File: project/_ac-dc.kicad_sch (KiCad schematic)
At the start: 27 parts

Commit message: adding more things and specifying components
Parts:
- removed R? (x2): 560K, symbol Device:R
- added C? (x2): 470n, symbol Device:C
- added C? (x2): 2n2, symbol Device:C
- added PS?: PSU 12V 1A, Converter_ACDC:Converter_ACDC_HiLink_HLK-PMxx, symbol Converter_ACDC:HLK-PM01
- added R? (x8): 220k, Resistor_SMD:R_0805_2012Metric_Pad1.20x1.40mm_HandSolder, symbol Device:R
- added RV?: 10D431K, Varistor:RV_Disc_D12mm_W5.4mm_P7.5mm, symbol Device:Varistor
- added TH?: 5D-15, Capacitor_THT:C_Disc_D12.5mm_W5.0mm_P7.50mm, symbol Device:Thermistor_NTC
- C? (x4): value 470u/200v -> 470u; Value2 (none) -> 200v
- C? (x10): value 47u/400v -> 47u; Value2 (none) -> 400v
- C? (x2): value 220u/400v -> 220u; Value2 (none) -> 400v
- TH?: value NTC -> 5D-15; footprint Capacitor_THT:C_Disc_D11.0mm_W5.0mm_P10.00mm -> Capacitor_THT:C_Disc_D12.5mm_W5.0mm_P7.50mm
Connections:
- net Earth: now also C?.1, C?.2
- net GND: now also PS?.2 (AC/N), PS?.3 (-Vout), R?.1
- net at C?.1, C?.1, C?.2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: now also R?.1, R?.1
- net at J?.3 (Pin_3), TH?.1: now also TH?.1
- net at D?.1 (K), D?.2, D?.2 (A)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: now also C?.1, C?.1, R?.1
- net at F?.2, FL?.2: now also C?.1, RV?.1
- net at D?.1 (K), D?.2 (A), D?.3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: now also C?.2, C?.2, R?.2
- net at FL?.1, TH?.2: now also C?.2, RV?.2, TH?.2
- net VCC renamed 320V
- net 320V: now also PS?.1 (AC/L), R?.1
- new net: R?.2, R?.2 (x2)
- new net: R?.1, R?.2 (x3)
- new net 12V: PS?.4 (+Vout)
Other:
- note added: "todo: * select last components * confirm footprints"
- moved on the sheet: C?, D?, F?, FL?, J?, TH?

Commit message: starting pcb
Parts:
- added L1: PFC, Connector:JWT_A3963_1x02_P3.96mm_Vertical, symbol Device:L_Iron
- CX1, CX2: renamed from C?; footprint (none) -> Capacitor_THT:C_Rect_L19.0mm_W9.0mm_P15.00mm_MKS4; Value3 X2 -> (none)
- CY1, CY2: renamed from C?; footprint (none) -> Capacitor_THT:C_Disc_D9.0mm_W5.0mm_P7.50mm; Value3 Y2 -> (none)
- FL1: renamed from FL?; footprint (none) -> -local:L_CommonMode_Toroid_Vertical_L34.3mm_W20.3mm_Px15.24mm_Py22.86mm_Bourns_8100; symbol Device:Filter_EMI_LL_1423 -> Device:Filter_EMI_CommonMode
- J1: renamed from J?; footprint (none) -> TerminalBlock_Phoenix:TerminalBlock_Phoenix_MKDS-1,5-3_1x03_P5.00mm_Horizontal
- gave numbers to parts that had none: 34
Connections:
- net E_AC_L: now reaches F1.1, J1.1 (Pin_1)
- net E_AC_N: now reaches J1.3 (Pin_3), TH1.1, TH2.1
- net AC_L: now reaches CX1.1, F1.2, RV1.1
- net AC_L: now also FL1.1; no longer FL1.2
- net AC_N: now reaches CX1.2, RV1.2, TH1.2, TH2.2
- net AC_N: now also FL1.3; no longer FL1.1
- net AC_N_F: now reaches CX2.2, CY2.2, D2.1 (K), D5.2 (A), FL1.4, R8.2
- net AC_N_F: now also D3.2; no longer D3.3
- new net AC_L_F: CX2.1, CY1.1, FL1.2, L1.1, R5.1
- new net AC_L_F_PFC: D1.1 (K), D3.3, D4.2 (A), L1.2
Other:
- note removed: "todo: * select last components * confirm footprints"
- company: (none) -> makerspace.lt
- title: (none) -> psu-500-pri

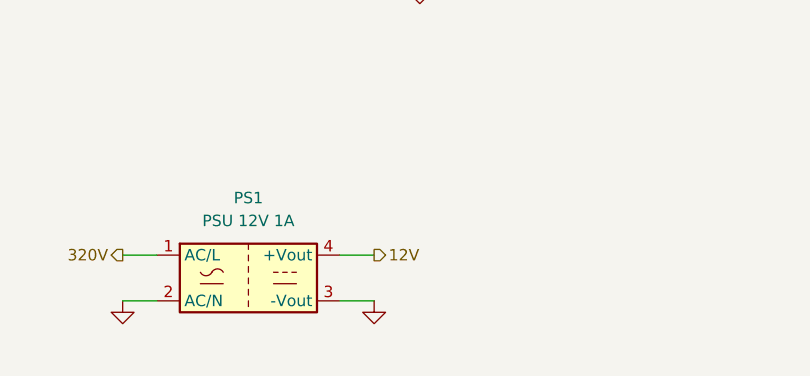
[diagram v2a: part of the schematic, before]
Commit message: finishing pcb
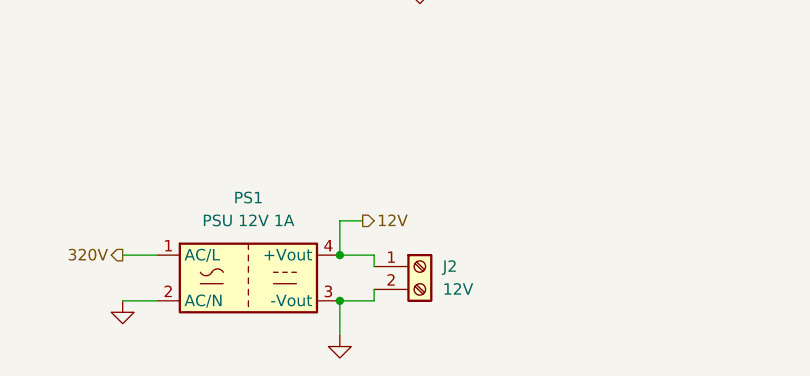
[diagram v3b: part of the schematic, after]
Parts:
- added J2: 12V, TerminalBlock_Phoenix:TerminalBlock_Phoenix_MKDS-1,5-2-5.08_1x02_P5.08mm_Horizontal, symbol Connector:Screw_Terminal_01x02
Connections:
- net 12V: now also J2.1 (Pin_1)
- net GND: now also J2.2 (Pin_2)

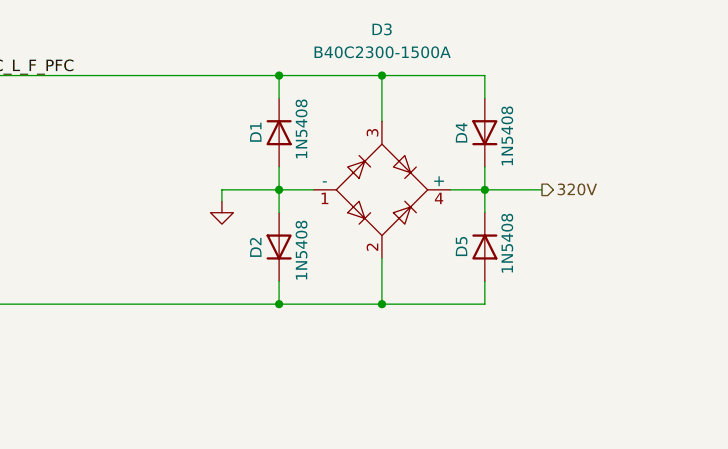
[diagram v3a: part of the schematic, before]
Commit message: adding few part numbers to the bom
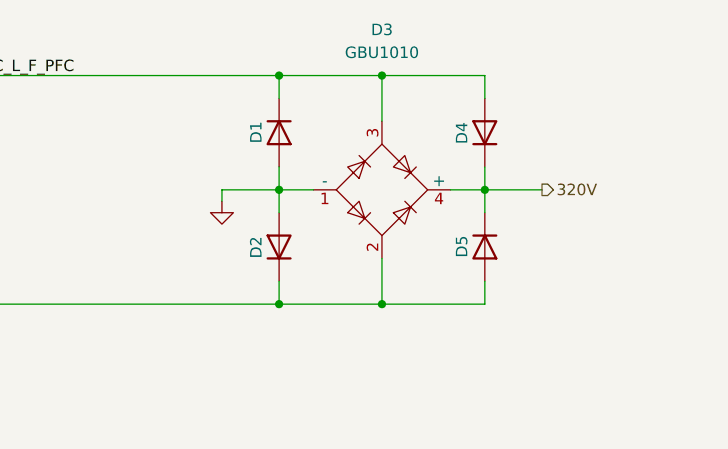
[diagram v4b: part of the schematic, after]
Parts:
- CX1, CX2: LCSC# (none) -> C5454415
- CY1, CY2: LCSC# (none) -> C5355118
- D1, D2, D4, D5: value 1N5408 -> ~
- D3: value B40C2300-1500A -> GBU1010; LCSC# (none) -> C5127096
- F1: LCSC# (none) -> C717030
- FL1: LCSC# (none) -> C2932158
- TH1, TH2: LCSC# (none) -> C2839620
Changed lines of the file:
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@@
       (effects (font (size 1.27 1.27)) (justify left))
     )
-    (property "Value" "1N5408" (id 1) (at 207.01 53.34 0)
+    (property "Value" "~" (id 1) (at 207.01 53.34 0)
       (effects (font (size 1.27 1.27)) (justify left))
     )
@@
       (effects (font (size 1.27 1.27)) hide)
     )
-    (property "Datasheet" "http://www.vishay.com/docs/88516/1n5400.pdf" (id 3) (at 204.47 57.15 0)
+    (property "Datasheet" "~" (id 3) (at 204.47 57.15 0)
       (effects (font (size 1.27 1.27)) hide)
     )
@@
     )
     (property "LCSC#" "C317794" (id 4) (at 77.47 63.5 90)
+      (effects (font (size 1.27 1.27)) hide)
+    )
+    (property "jlc-part-type" "" (id 5) (at 77.47 63.5 0)
       (effects (font (size 1.27 1.27)) hide)
     )
@@
       (effects (font (size 1.27 1.27)) hide)
     )
-    (property "Datasheet" "~" (id 3) (at 114.3 63.5 0)
+    (property "Datasheet" "https://datasheet.lcsc.com/lcsc/C5454415.pdf" (id 3) (at 114.3 63.5 0)
       (effects (font (size 1.27 1.27)) hide)
     )
     (property "Value2" "250V~" (id 4) (at 120.65 66.04 0))
+    (property "LCSC#" "C5454415" (id 5) (at 114.3 63.5 0)
+      (effects (font (size 1.27 1.27)) hide)
+    )
+    (property "jlc-part-type" "" (id 6) (at 114.3 63.5 0)
+      (effects (font (size 1.27 1.27)) hide)
+    )
     (pin "1")
     (pin "2")
@@
       (effects (font (size 1.27 1.27)) hide)
     )
-    (property "Datasheet" "~" (id 3) (at 68.58 50.8 0)
+    (property "Datasheet" "https://datasheet.lcsc.com/lcsc/C717030.pdf" (id 3) (at 68.58 50.8 0)
+      (effects (font (size 1.27 1.27)) hide)
+    )
+    (property "LCSC#" "C717030" (id 4) (at 68.58 50.8 90)
+      (effects (font (size 1.27 1.27)) hide)
+    )
+    (property "jlc-part-type" "" (id 5) (at 68.58 50.8 0)
       (effects (font (size 1.27 1.27)) hide)
     )
@@
       (effects (font (size 1.27 1.27)) hide)
     )
-    (property "Datasheet" "~" (id 3) (at 149.86 69.85 0)
+    (property "Datasheet" "https://datasheet.lcsc.com/lcsc/C5355118.pdf" (id 3) (at 149.86 69.85 0)
       (effects (font (size 1.27 1.27)) hide)
     )
     (property "Value2" "250V~" (id 4) (at 156.21 72.39 0))
+    (property "LCSC#" "C5355118" (id 5) (at 149.86 69.85 0)
+      (effects (font (size 1.27 1.27)) hide)
+    )
+    (property "jlc-part-type" "" (id 6) (at 149.86 69.85 0)
+      (effects (font (size 1.27 1.27)) hide)
+    )
     (pin "1")
     (pin "2")
@@
       (effects (font (size 1.27 1.27)) hide)
     )
-    (property "Datasheet" "~" (id 3) (at 69.85 83.82 0)
+    (property "Datasheet" "https://datasheet.lcsc.com/lcsc/C2839620.pdf" (id 3) (at 69.85 83.82 0)
+      (effects (font (size 1.27 1.27)) hide)
+    )
+    (property "LCSC#" "C2839620" (id 4) (at 71.12 83.82 90)
+      (effects (font (size 1.27 1.27)) hide)
+    )
+    (property "jlc-part-type" "" (id 5) (at 71.12 83.82 0)
       (effects (font (size 1.27 1.27)) hide)
     )
@@
       (effects (font (size 1.27 1.27)) (justify left))
     )
-    (property "Value" "1N5408" (id 1) (at 229.87 66.04 0)
+    (property "Value" "~" (id 1) (at 229.87 66.04 0)
       (effects (font (size 1.27 1.27)) (justify left))
     )
@@
       (effects (font (size 1.27 1.27)) hide)
     )
-    (property "Datasheet" "http://www.vishay.com/docs/88516/1n5400.pdf" (id 3) (at 227.33 69.85 0)
+    (property "Datasheet" "~" (id 3) (at 227.33 69.85 0)
       (effects (font (size 1.27 1.27)) hide)
     )
@@
     (in_bom yes) (on_board yes)
     (property "Reference" "D3" (id 0) (at 215.9 45.72 0))
-    (property "Value" "B40C2300-1500A" (id 1) (at 215.9 48.26 0))
+    (property "Value" "GBU1010" (id 1) (at 215.9 48.26 0))
     (property "Footprint" "Diode_THT:Diode_Bridge_19.0x3.5x10.0mm_P5.0mm" (id 2) (at 219.71 66.675 0)
       (effects (font (size 1.27 1.27)) (justify left) hide)
     )
-    (property "Datasheet" "https://diotec.com/tl_files/diotec/files/pdf/datasheets/b40c2300.pdf" (id 3) (at 215.9 63.5 0)
+    (property "Datasheet" "https://datasheet.lcsc.com/lcsc/2208121800_SEP-GBU1010_C5127096.pdf" (id 3) (at 215.9 63.5 0)
+      (effects (font (size 1.27 1.27)) hide)
+    )
+    (property "LCSC#" "C5127096" (id 4) (at 215.9 63.5 0)
+      (effects (font (size 1.27 1.27)) hide)
+    )
+    (property "jlc-part-type" "" (id 5) (at 215.9 63.5 0)
       (effects (font (size 1.27 1.27)) hide)
     )
@@
       (effects (font (size 1.27 1.27)) hide)
     )
-    (property "Datasheet" "~" (id 3) (at 149.86 57.15 0)
+    (property "Datasheet" "https://datasheet.lcsc.com/lcsc/C5355118.pdf" (id 3) (at 149.86 57.15 0)
       (effects (font (size 1.27 1.27)) hide)
     )
     (property "Value2" "250V~" (id 4) (at 156.21 59.69 0))
+    (property "LCSC#" "C5355118" (id 5) (at 149.86 57.15 0)
+      (effects (font (size 1.27 1.27)) hide)
+    )
+    (property "jlc-part-type" "" (id 6) (at 149.86 57.15 0)
+      (effects (font (size 1.27 1.27)) hide)
+    )
     (pin "1")
     (pin "2")
@@
       (effects (font (size 1.27 1.27)) (justify left))
     )
-    (property "Value" "1N5408" (id 1) (at 207.01 73.66 0)
+    (property "Value" "~" (id 1) (at 207.01 73.66 0)
       (effects (font (size 1.27 1.27)) (justify left))
     )
@@
       (effects (font (size 1.27 1.27)) hide)
     )
-    (property "Datasheet" "http://www.vishay.com/docs/88516/1n5400.pdf" (id 3) (at 204.47 69.85 0)
+    (property "Datasheet" "~" (id 3) (at 204.47 69.85 0)
       (effects (font (size 1.27 1.27)) hide)
     )
@@
       (effects (font (size 1.27 1.27)) hide)
     )
-    (property "Datasheet" "~" (id 3) (at 69.85 76.2 0)
+    (property "Datasheet" "https://datasheet.lcsc.com/lcsc/C2839620.pdf" (id 3) (at 69.85 76.2 0)
+      (effects (font (size 1.27 1.27)) hide)
+    )
+    (property "LCSC#" "C2839620" (id 4) (at 71.12 76.2 90)
+      (effects (font (size 1.27 1.27)) hide)
+    )
+    (property "jlc-part-type" "" (id 5) (at 71.12 76.2 0)
       (effects (font (size 1.27 1.27)) hide)
     )
@@
       (effects (font (size 1.27 1.27)) (justify left))
     )
-    (property "Value" "1N5408" (id 1) (at 229.87 60.96 0)
+    (property "Value" "~" (id 1) (at 229.87 60.96 0)
       (effects (font (size 1.27 1.27)) (justify left))
     )
@@
       (effects (font (size 1.27 1.27)) hide)
     )
-    (property "Datasheet" "http://www.vishay.com/docs/88516/1n5400.pdf" (id 3) (at 227.33 57.15 0)
+    (property "Datasheet" "~" (id 3) (at 227.33 57.15 0)
       (effects (font (size 1.27 1.27)) hide)
     )
@@
       (effects (font (size 1.27 1.27)) hide)
     )
-    (property "Datasheet" "~" (id 3) (at 104.14 62.484 0)
+    (property "Datasheet" "https://datasheet.lcsc.com/lcsc/2201121530_PROD-Tech-PDUUAT105-202MLN_C2932158.pdf" (id 3) (at 104.14 62.484 0)
+      (effects (font (size 1.27 1.27)) hide)
+    )
+    (property "LCSC#" "C2932158" (id 4) (at 104.14 63.5 0)
+      (effects (font (size 1.27 1.27)) hide)
+    )
+    (property "jlc-part-type" "" (id 5) (at 104.14 63.5 0)
       (effects (font (size 1.27 1.27)) hide)
     )
@@
       (effects (font (size 1.27 1.27)) hide)
     )
-    (property "Datasheet" "~" (id 3) (at 87.63 63.5 0)
+    (property "Datasheet" "https://datasheet.lcsc.com/lcsc/C5454415.pdf" (id 3) (at 87.63 63.5 0)
       (effects (font (size 1.27 1.27)) hide)
     )
     (property "Value2" "250V~" (id 4) (at 93.98 66.04 0))
-    (pin "1")
-    (pin "2")
+    (property "LCSC#" "C5454415" (id 5) (at 87.63 63.5 0)
+      (effects (font (size 1.27 1.27)) hide)
+    )
+    (property "jlc-part-type" "" (id 6) (at 87.63 63.5 0)
+      (effects (font (size 1.27 1.27)) hide)
+    )
+    (pin "1")
+    (pin "2")
